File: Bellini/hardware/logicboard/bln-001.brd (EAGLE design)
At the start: 91 x 90 mm, 49 parts, among them IC1 74ACT06N, J1 MKR, J10 THS, J16 MNTR, J2 GPIO, J20 GPIO, J21 Grove, J22 Grove, J23 Grove, J24 Grove, J5 SPI, J6 LED, J7 DIN5, J8 DIN5, J9 DIN5, K1 G5V1, T1 2SC1815, X3 FAN

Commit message: Prototyping...
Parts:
- removed B0: 0, rcl:M3216
- removed C11: 100n, rcl:C025-024X044
- removed C12, C13: 1u, rcl:C050-024X044
- removed D2, D3, D4: (no value), SparkFun-DiscreteSemi:DIODE-1N4148
- removed DISP1: AQM0802A-RN-GBW, AQM0802A-RN-GBW:AQM0802A-RN-GBW-FOOTPRINT
- removed IC1: 74ACT06N, 74xx-eu:DIL14
- removed J1: MKR, SparkFun-Connectors:JST-5-PTH
- removed J10: THS, SparkFun-Connectors:JST-3-PTH-VERT
- removed J16: MNTR, SparkFun-Connectors:JST-2-PTH-NS
- removed J2: GPIO, SparkFun-Connectors:JST-4-PTH
- removed J20: GPIO, SparkFun-Connectors:1X04_1.27MM
- removed J5: SPI, SparkFun-Connectors:1X06_1.27MM
- removed J6: LED, SparkFun-Connectors:JST-3-PTH-VERT
- removed J7, J8, J9: DIN5, SparkFun-Connectors:DIN5-RA-PTH
- removed JP8: Extended GPIO, SparkFun-Connectors:1X10_LOCK
- removed K1: G5V1, relay:G5V1
- removed LED0: Green, led:KA-3528ASYC
- removed LED1: Red, led:KA-3528ASYC
- removed OK1: HCPL2630, optocoupler:DIL08
- removed R1, R4, R5: 1k, resistor:0204/5
- removed R2: 10k, resistor:0204/5
- removed RN2, RN3: 4.7k, resistor-net:RN-5
- removed RN4: 220, resistor-dil:DIL16
- removed T1: 2SC1815, transistor:TO92-ECB
- removed X3: FAN, pinhead:2X02
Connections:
- removed net BASE: R1.1, R2.2, T1.B
- removed net CAP1N: C12.2, DISP1.3
- removed net CAP1P: C12.1, DISP1.4
- removed net COLLECTOR: D2.A, K1.9, T1.C
- removed net COMMON: K1.5, K1.6, X3.2
- removed net FANDRIVE: B0.2, K1.10, X3.4
- removed net LCDVOUT: C13.2, DISP1.2
- removed net LED0A: J6.3, LED0.A, R4.1
- removed net LED1A: J6.1, LED1.A, R5.1
- removed net MIDIINSND: D3.C, OK1.1, RN4.2
- removed net MIRTN: D3.A, J7.5, OK1.2
- removed net MISND: J7.4, RN4.15
- removed net MNTRA: J16.2, RN4.1
- removed net MNTRAA: D4.C, OK1.4, RN4.16
- removed net MNTRK: D4.A, J16.1, OK1.3
- removed net MO2RTN: RN4.9
- removed net MO2RTNRAW: IC1.12, RN4.8
- removed net MO2SND: RN4.10
- removed net MORTN: J9.5, RN4.13
- removed net MORTNRAW: IC1.10, RN4.4
- removed net MOSND: J9.4, RN4.14
- removed net MTRTN: J8.5, RN4.11
- removed net MTRTNRAW: IC1.8, RN4.6
- removed net MTSND: J8.4, RN4.12
- removed net NMO2RTN: IC1.13, IC1.6, RN2.5
- removed net NMORTN: IC1.11, IC1.4, RN2.4
- removed net NMTRTN: IC1.2, IC1.9, RN2.3
- net DIGITAL7: no longer J1.4
- net GND: no longer C11.2, DISP1.6, IC1.7, J1.1, J10.1, J2.1, J5.6, J6.2, J8.2, J9.2, JP8.1, K1.1, LED0.C, LED1.C, OK1.5, R2.1, T1.E, X3.1
- net GPIO0: no longer J2.3, J20.3
- net GPIO1: no longer J2.4, J20.4
- net GPIO2: no longer JP8.3
- net GPIO3: no longer JP8.4
- net GPIO4: no longer JP8.5
- net GPIO5: no longer JP8.6
- net GPIO6: no longer JP8.7
- net GPIO7: no longer JP8.8
- net LED0: no longer R4.2
- net LED1: no longer R5.2
- net MISO: no longer J5.1
- net MNTR: no longer OK1.6, RN3.5
- net MOSI: no longer J5.4
- net RLY: no longer R1.2
- net RST: no longer J5.5
- net RX: no longer IC1.1, OK1.7, RN3.4
- net SCK: no longer J5.3
- net SCL: no longer DISP1.8, J1.3
- net SDA: no longer DISP1.7, J1.2
- net THS: no longer J10.2, RN3.3
- net TX: no longer IC1.3, IC1.5
- net VCC: no longer B0.1, IC1.14, RN2.1, RN4.3, RN4.5, RN4.7, X3.3
- net VDD: no longer C11.1, C13.1, D2.C, DISP1.5, DISP1.9, J1.5, J10.3, J2.2, J5.2, JP8.2, K1.2, OK1.8, RN3.1
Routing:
- net GND: track 479.7 -> 0.00 mm, vias 3 -> 0
- net VDD: track 330.9 -> 0.00 mm, vias 4 -> 0
- net SDA: track 259.0 -> 0.00 mm, vias 4 -> 0
- net SCL: track 238.5 -> 0.00 mm, vias 3 -> 0
- net VCC: track 144.6 -> 0.00 mm, vias 2 -> 0
- net RX: track 140.7 -> 0.00 mm, vias 1 -> 0
- net NMO2RTN: track 123.2 -> 0.00 mm, vias 1 -> 0
- net DIGITAL7: track 117.3 -> 0.00 mm, vias 2 -> 0
- net GPIO3: track 112.9 -> 0.00 mm, vias 2 -> 0
- net GPIO7: track 110.2 -> 0.00 mm, vias 2 -> 0
- net THS: track 106.9 -> 0.00 mm, vias 3 -> 0
- net NMTRTN: track 106.5 -> 0.00 mm, vias 4 -> 0
- net NMORTN: track 102.3 -> 0.00 mm, vias 1 -> 0
- net GPIO6: track 100.3 -> 0.00 mm, vias 2 -> 0
- net TX: track 98.5 -> 0.00 mm
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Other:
- board text removed: "0"
- board text removed: "102"
- board text removed: "104"
- board text removed: "2-472"
- board text removed: "221"
- board text removed: "331"
- board text removed: "4"
- board text removed: "5"
- board text removed: "74HCT05 (5V)"
- board text removed: "Akizuki AQM0802A-RN-GBW"
- board text removed: "BRIDGE*"
- board text removed: "C"
- board text removed: "Configuration of X3"
- board text removed: "DS18B20+"
- board text removed: "Fan GND"
- board text removed: "Fan Vcc"
- board text removed: "G5V-1"
- board text removed: "I"
- board text removed: "L0"
- board text removed: "L1"
- board text removed: "N"
- board text removed: "NO"
- board text removed: "RLY"
- board text removed: "RLY-A"
- board text removed: "RLY-B"
- board text removed: "RTN"
- board text removed: "SND"
- board text removed: "TLP2630"
- board text removed: "TO FAN*"

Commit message: Changed dimension.
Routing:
- removed copper zone on layer 1, net GND
- removed copper zone on layer 16, net GND
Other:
- board size 91 x 90 mm -> 100 x 80 mm
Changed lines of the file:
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@@
 <setting verticaltext="up"/>
 </settings>
-<grid distance="0.5" unitdist="mm" unit="mm" style="lines" multiple="2" display="yes" altdistance="50" altunitdist="mil" altunit="mil"/>
+<grid distance="5" unitdist="mm" unit="mm" style="lines" multiple="2" display="yes" altdistance="50" altunitdist="mil" altunit="mil"/>
 <layers>
 <layer number="1" name="Top" color="4" fill="1" visible="yes" active="yes"/>
@@
 <board>
 <plain>
-<wire x1="78" y1="90" x2="13" y2="90" width="0" layer="20"/>
-<wire x1="13" y1="90" x2="12" y2="89" width="0" layer="20" curve="90"/>
-<wire x1="12" y1="89" x2="12" y2="80" width="0" layer="20"/>
-<wire x1="10.5" y1="78.5" x2="1" y2="78.5" width="0" layer="20"/>
-<wire x1="1" y1="78.5" x2="0" y2="77.5" width="0" layer="20" curve="90"/>
-<wire x1="0" y1="77.5" x2="0" y2="12.5" width="0" layer="20"/>
-<wire x1="0" y1="12.5" x2="1" y2="11.5" width="0" layer="20" curve="90"/>
-<wire x1="1" y1="11.5" x2="10.5" y2="11.5" width="0" layer="20"/>
-<wire x1="12" y1="10" x2="12" y2="1" width="0" layer="20"/>
-<wire x1="12" y1="1" x2="13" y2="0" width="0" layer="20" curve="90"/>
-<wire x1="13" y1="0" x2="78" y2="0" width="0" layer="20"/>
-<wire x1="78" y1="0" x2="79" y2="1" width="0" layer="20" curve="90"/>
-<wire x1="79" y1="1" x2="79" y2="10" width="0" layer="20"/>
-<wire x1="80.5" y1="11.5" x2="90" y2="11.5" width="0" layer="20"/>
-<wire x1="90" y1="11.5" x2="91" y2="12.5" width="0" layer="20" curve="90"/>
-<wire x1="91" y1="12.5" x2="91" y2="77.5" width="0" layer="20"/>
-<wire x1="91" y1="77.5" x2="90" y2="78.5" width="0" layer="20" curve="90"/>
-<wire x1="90" y1="78.5" x2="80.5" y2="78.5" width="0" layer="20"/>
-<wire x1="79" y1="80" x2="79" y2="89" width="0" layer="20"/>
-<wire x1="79" y1="89" x2="78" y2="90" width="0" layer="20" curve="90"/>
+<wire x1="98" y1="80" x2="2" y2="80" width="0" layer="20"/>
+<wire x1="2" y1="80" x2="0" y2="78" width="0" layer="20" curve="90"/>
+<wire x1="0" y1="78" x2="0" y2="2" width="0" layer="20"/>
+<wire x1="0" y1="2" x2="2" y2="0" width="0" layer="20" curve="90"/>
+<wire x1="2" y1="0" x2="98" y2="0" width="0" layer="20"/>
+<wire x1="98" y1="0" x2="100" y2="2" width="0" layer="20" curve="90"/>
+<wire x1="100" y1="2" x2="100" y2="78" width="0" layer="20"/>
+<wire x1="100" y1="78" x2="98" y2="80" width="0" layer="20" curve="90"/>
 <hole x="76.5" y="76" drill="2.5"/>
 <circle x="14.5" y="14" radius="2.6" width="0.2" layer="42"/>
@@
 <circle x="76.5" y="14" radius="2.6" width="0.2" layer="41"/>
 <text x="45.5" y="20.5" size="1.27" layer="25" align="center">Sweetio 0.0.2-X</text>
-<wire x1="79" y1="80" x2="80.5" y2="78.5" width="0" layer="20" curve="90"/>
-<wire x1="12" y1="80" x2="10.5" y2="78.5" width="0" layer="20" curve="-90"/>
-<wire x1="79" y1="10" x2="80.5" y2="11.5" width="0" layer="20" curve="-90"/>
-<wire x1="10.5" y1="11.5" x2="12" y2="10" width="0" layer="20" curve="-90"/>
 <hole x="14.5" y="76" drill="2.5"/>
 <hole x="14.5" y="14" drill="2.5"/>
 <hole x="76.5" y="14" drill="2.5"/>
-<rectangle x1="12" y1="89" x2="79" y2="90" layer="41"/>
-<rectangle x1="90" y1="11.5" x2="91" y2="78.5" layer="41"/>
+<rectangle x1="14" y1="92" x2="81" y2="93" layer="41"/>
+<rectangle x1="115" y1="11.5" x2="116" y2="78.5" layer="41"/>
 <rectangle x1="12" y1="0" x2="79" y2="1" layer="41"/>
-<rectangle x1="0" y1="11.5" x2="1" y2="78.5" layer="41"/>
-<rectangle x1="0" y1="77.5" x2="12" y2="78.5" layer="41"/>
-<rectangle x1="12" y1="78.5" x2="13" y2="90" layer="41"/>
-<rectangle x1="78" y1="78.5" x2="79" y2="90" layer="41"/>
-<rectangle x1="79" y1="77.5" x2="91" y2="78.5" layer="41"/>
-<rectangle x1="79" y1="11.5" x2="91" y2="12.5" layer="41"/>
-<rectangle x1="78" y1="0" x2="79" y2="11.5" layer="41"/>
-<rectangle x1="12" y1="0" x2="13" y2="11.5" layer="41"/>
-<rectangle x1="0" y1="11.5" x2="12" y2="12.5" layer="41"/>
-<rectangle x1="78" y1="0" x2="79" y2="11.5" layer="42"/>
-<rectangle x1="79" y1="11.5" x2="91" y2="12.5" layer="42"/>
-<rectangle x1="90" y1="11.5" x2="91" y2="78.5" layer="42"/>
-<rectangle x1="79" y1="77.5" x2="91" y2="78.5" layer="42"/>
-<rectangle x1="78" y1="78.5" x2="79" y2="90" layer="42"/>
-<rectangle x1="12" y1="89" x2="79" y2="90" layer="42"/>
-<rectangle x1="12" y1="78.5" x2="13" y2="90" layer="42"/>
-<rectangle x1="0" y1="77.5" x2="12" y2="78.5" layer="42"/>
-<rectangle x1="0" y1="11.5" x2="1" y2="78.5" layer="42"/>
-<rectangle x1="0" y1="11.5" x2="12" y2="12.5" layer="42"/>
-<rectangle x1="12" y1="0" x2="13" y2="11.5" layer="42"/>
+<rectangle x1="-10" y1="11.5" x2="-9" y2="78.5" layer="41"/>
+<rectangle x1="-8" y1="90.5" x2="4" y2="91.5" layer="41"/>
+<rectangle x1="4" y1="81" x2="5" y2="92.5" layer="41"/>
+<rectangle x1="85.5" y1="77.5" x2="86.5" y2="89" layer="41"/>
+<rectangle x1="79.5" y1="74" x2="91.5" y2="75" layer="41"/>
+<rectangle x1="76.5" y1="11" x2="88.5" y2="12" layer="41"/>
+<rectangle x1="61" y1="2.5" x2="62" y2="14" layer="41"/>
+<rectangle x1="22" y1="5" x2="23" y2="16.5" layer="41"/>
+<rectangle x1="20" y1="11.5" x2="32" y2="12.5" layer="41"/>
+<rectangle x1="47.5" y1="8" x2="48.5" y2="19.5" layer="42"/>
+<rectangle x1="78" y1="13" x2="90" y2="14" layer="42"/>
+<rectangle x1="110" y1="11.5" x2="111" y2="78.5" layer="42"/>
+<rectangle x1="79.5" y1="75" x2="91.5" y2="76" layer="42"/>
+<rectangle x1="84" y1="78.5" x2="85" y2="90" layer="42"/>
+<rectangle x1="9.5" y1="90.5" x2="76.5" y2="91.5" layer="42"/>
+<rectangle x1="3" y1="82" x2="4" y2="93.5" layer="42"/>
+<rectangle x1="-6" y1="84.5" x2="6" y2="85.5" layer="42"/>
+<rectangle x1="-5" y1="11.5" x2="-4" y2="78.5" layer="42"/>
+<rectangle x1="15" y1="16.5" x2="27" y2="17.5" layer="42"/>
+<rectangle x1="32" y1="5" x2="33" y2="16.5" layer="42"/>
 <rectangle x1="12" y1="0" x2="79" y2="1" layer="42"/>
 <text x="0.5" y="14.5" size="1" layer="25" align="center-left">Designed for
@@
 <contactref element="J23" pad="4"/>
 <contactref element="J24" pad="4"/>
-<polygon width="0.2" layer="1">
-<vertex x="-1" y="-1"/>
-<vertex x="92" y="-1"/>
-<vertex x="92" y="91"/>
-<vertex x="-1" y="91"/>
-</polygon>
-<polygon width="0.2" layer="16">
-<vertex x="-2" y="-2"/>
-<vertex x="93" y="-2"/>
-<vertex x="93" y="92"/>
-<vertex x="-2" y="92"/>
-</polygon>
 <wire x1="58" y1="80.5" x2="69" y2="80.5" width="0" layer="19" extent="1-1"/>
 <wire x1="59.225" y1="64.08" x2="58" y2="80.5" width="0" layer="19" extent="1-1"/>

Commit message: Cleaning.
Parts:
- removed H1, H2: STAND-OFF, SparkFun-Hardware:STAND-OFF
- removed J23, J24: Grove, Connector:4P-2.0-W/O-BUCKLE
- removed JP2: RTC, SparkFun-Connectors:1X05
- removed SV3: Testport II, pinhead:2X07
- added JP01: (no value), pinhead:2X05
- moved J22 80.8 mm to (25.0, 5.50)
- moved J21 79.1 mm to (41.0, 5.50)
- moved C6 70.7 mm to (87.5, 36.0)
- moved LOGO1 63.7 mm to (50.0, 10.0), flipped to the top
- moved U$1 33.3 mm to (50.0, 20.0)
- moved S1 27.7 mm to (50.0, 76.0)
- moved C5 22.4 mm to (75.5, 32.0)
- moved MC2 11.0 mm to (50.0, 64.0)
- moved JP00 4.61 mm to (5.00, 64.0), turned to 90 degrees
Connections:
- net DIGITAL7: no longer SV3.11
- net DTCT0: no longer SV3.8
- net DTCT1: no longer SV3.10
- net DTCT2: no longer SV3.12
- net DTCT3: no longer SV3.14
- net GND: no longer J23.4, J24.4, JP2.2, SV3.5
- net GPIO0: no longer SV3.2
- net GPIO1: no longer SV3.4
- net RX: no longer SV3.3
- net SCL: no longer J23.1, J24.1, JP2.4, SV3.9
- net SDA: no longer J23.2, J24.2, JP2.5, SV3.7
- net THS: no longer SV3.6
- net TX: no longer SV3.1
- net VDD: no longer J23.3, J24.3, JP2.1, SV3.13
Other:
- board text added: "Bellini Prototype 00"
- board text removed: "1"
- board text removed: "2"
- board text removed: "2-Grove"
- board text removed: "SC"
- board text removed: "SD"
- board text removed: "SparkFun Real Time Clock Module (12708)"
- board text removed: "Sweetio 0.0.2-X"
- board text removed: "TestPort II"
- board text removed: "To RUN Pad (RPiZW2)"

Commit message: Layout.
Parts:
- removed J22: Grove, Connector:4P-2.0-90D
- added JP02, JP03: (no value), adafruit:1X08-BIG
- added JP04, JP05: (no value), pinhead:1X14
- moved JP01 70.0 mm to (15.0, 20.0)
- moved C6 61.0 mm to (27.5, 25.0)
- moved C7 60.8 mm to (14.5, 64.0)
- moved J21 26.2 mm to (15.0, 9.00), turned to 180 degrees
- moved U$1 20.0 mm to (50.0, 40.0), flipped to the bottom
- moved C5 14.2 mm to (81.2, 45.0)
- moved LOGO1 7.00 mm to (50.0, 3.00)
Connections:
- net GND: no longer J22.4
- net SCL: no longer J22.1
- net SDA: no longer J22.2
- net VDD: no longer J22.3

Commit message: Routed.
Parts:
- removed JP01: (no value), pinhead:2X05
- added LEVELSHIFT1, LEVELSHIFT2: (no value), pinhead:1X04
- added RTCPIN: (no value), pinhead:2X05
- turned DRIVERPIN1 to 270 degrees
- turned LEDPIN2 to 270 degrees
- renumbered J21 to GROVE1, JP02 to LEDPIN1, JP03 to LEDPIN2, JP04 to DRIVERPIN1, JP05 to DRIVERPIN2
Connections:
- removed net DTCT0: MC2.15
- removed net DTCT1: MC2.16
- removed net DTCT2: MC2.18
- removed net DTCT3: MC2.22
- removed net GPIO0: MC2.38
- removed net GPIO1: MC2.40
- removed net GPIO2: MC2.24
- removed net GPIO3: MC2.36
- removed net GPIO4: MC2.11
- removed net GPIO5: MC2.12
- removed net GPIO6: MC2.35
- removed net GPIO7: MC2.37
- removed net LED0: MC2.32
- removed net LED1: MC2.33
- removed net MISO: MC2.21
- removed net MNTR: MC2.31
- removed net MOSI: MC2.19
- removed net RLY: MC2.29
- removed net SCK: MC2.23
- removed net THS: MC2.7
- new net COL1: DRIVERPIN2.11, LEDPIN2.5
- new net COL2: DRIVERPIN2.10, LEDPIN1.3
- new net COL3: DRIVERPIN2.9, LEDPIN1.4
- new net COL4: DRIVERPIN2.8, LEDPIN2.3
- new net COL5: DRIVERPIN2.7, LEDPIN1.6
- new net COL6: DRIVERPIN2.6
- new net COL7: DRIVERPIN2.5, LEDPIN2.7
- new net COL8: DRIVERPIN2.4, LEDPIN2.8
- new net N$10: DRIVERPIN1.11
- new net N$11: DRIVERPIN1.12
- new net N$12: DRIVERPIN1.13
- new net N$13: DRIVERPIN1.14
- new net N$14: DRIVERPIN2.1
- new net N$15: DRIVERPIN2.2
- new net N$16: DRIVERPIN2.3
- new net N$5: LEVELSHIFT1.4
- new net N$9: DRIVERPIN1.10
- new net ROW1: DRIVERPIN1.2, LEDPIN2.1
- new net ROW2: DRIVERPIN1.3, LEDPIN2.6
- new net ROW3: DRIVERPIN1.4, LEDPIN1.8
- new net ROW4: DRIVERPIN1.5, LEDPIN2.4
- new net ROW5: DRIVERPIN1.6, LEDPIN1.1
- new net ROW6: DRIVERPIN1.7, LEDPIN1.7
- new net ROW7: DRIVERPIN1.8, LEDPIN1.2, LEDPIN2.2
- new net ROW8: DRIVERPIN1.9, LEDPIN1.5
- new net SCL5V: DRIVERPIN2.12, LEVELSHIFT2.3
- new net SDA5V: DRIVERPIN2.13, LEVELSHIFT2.2
- net DIGITAL7: now also RTCPIN.7
- net GND: now also DRIVERPIN1.1, LEVELSHIFT2.1, RTCPIN.6, RTCPIN.9; no longer MC2.25
- net RX: now also RTCPIN.10
- net SCL: now also LEVELSHIFT1.2, RTCPIN.5
- net SDA: now also LEVELSHIFT1.3, RTCPIN.3
- net TX: now also RTCPIN.8
- net VCC: now also DRIVERPIN2.14, LEVELSHIFT2.4, RTCPIN.2, RTCPIN.4
- net VDD: now also LEVELSHIFT1.1, RTCPIN.1
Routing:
- net GND: track 0.00 -> 227.3 mm
- net VDD: track 0.00 -> 176.4 mm
- net SCL: track 0.00 -> 115.4 mm
- net SDA: track 0.00 -> 114.3 mm
- net VCC: track 0.00 -> 103.0 mm
- net COL5: track 0.00 -> 69.5 mm
- net COL2: track 0.00 -> 68.2 mm
- net COL3: track 0.00 -> 66.0 mm
- net TX: track 0.00 -> 61.9 mm
- net RX: track 0.00 -> 59.1 mm
- net RST: track 0.00 -> 54.3 mm
- net ROW7: track 0.00 -> 50.4 mm
- net ROW5: track 0.00 -> 49.1 mm
- net ROW6: track 0.00 -> 39.6 mm
- net ROW8: track 0.00 -> 38.7 mm
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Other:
- board text added: "1"
- board text added: "4-M3"
- board text added: "Bellini Prototype 00 v1.0"
- board text added: "Designed for Takachi SKL10-5-10"
- board text added: "HT16K33 Breakout"
- board text added: "OptoSuply OSL641501"
- board text added: "PCA9306 Breakout"
- board text removed: "103"
- board text removed: "4-M2.3"
- board text removed: "Bellini Prototype 00"
- board text removed: "Designed for Takachi PF10-4-10"

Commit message: Fixed errors.
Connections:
- net COL1 renamed A0
- net COL2 renamed A1
- net COL3 renamed A2
- net COL5 renamed A4
- net COL7 renamed A6
- net COL8 renamed A7
- net ROW1 renamed C0
- net ROW2 renamed C1
- net ROW3 renamed C2
- net ROW4 renamed C3
- net ROW5 renamed C4
- net ROW6 renamed C5
- net ROW8 renamed C7
- removed net COL4: DRIVERPIN2.8, LEDPIN2.3
- removed net COL6: DRIVERPIN2.6
- removed net ROW7: DRIVERPIN1.8, LEDPIN1.2, LEDPIN2.2
- new net A3: DRIVERPIN2.8, LEDPIN2.2
- new net A5: DRIVERPIN2.6, LEDPIN2.3
- new net C6: DRIVERPIN1.8, LEDPIN1.2
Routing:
- net ROW7: track 50.4 -> 0.00 mm
- net C6: track 0.00 -> 38.7 mm
- net A5: track 0.00 -> 32.1 mm
- net COL4: track 30.0 -> 0.00 mm
- net A3: track 0.00 -> 29.2 mm
- net VDD: track 176.4 -> 162.1 mm, vias 0 -> 2
- net SCL: track 115.4 -> 119.3 mm
- net SDA: track 114.3 -> 117.8 mm
- net A2: track 66.0 -> 69.4 mm
- net TX: track 61.9 -> 59.9 mm, vias 0 -> 1
- net DIGITAL7: track 35.2 -> 36.7 mm
- net A0: track 37.1 -> 38.4 mm
- added copper zone on layer 1, net GND
- added copper zone on layer 16, net GND

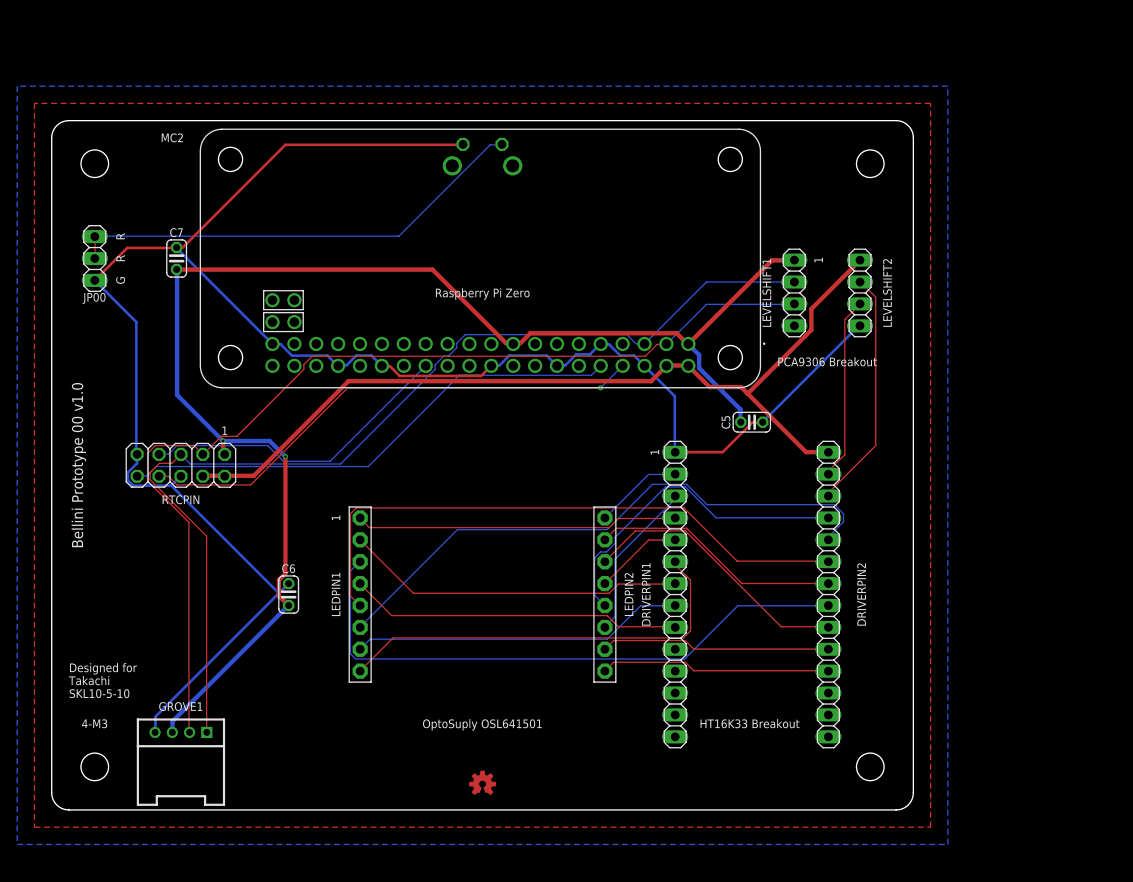
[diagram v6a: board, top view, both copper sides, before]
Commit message: Fixed direction of Pi RTC.
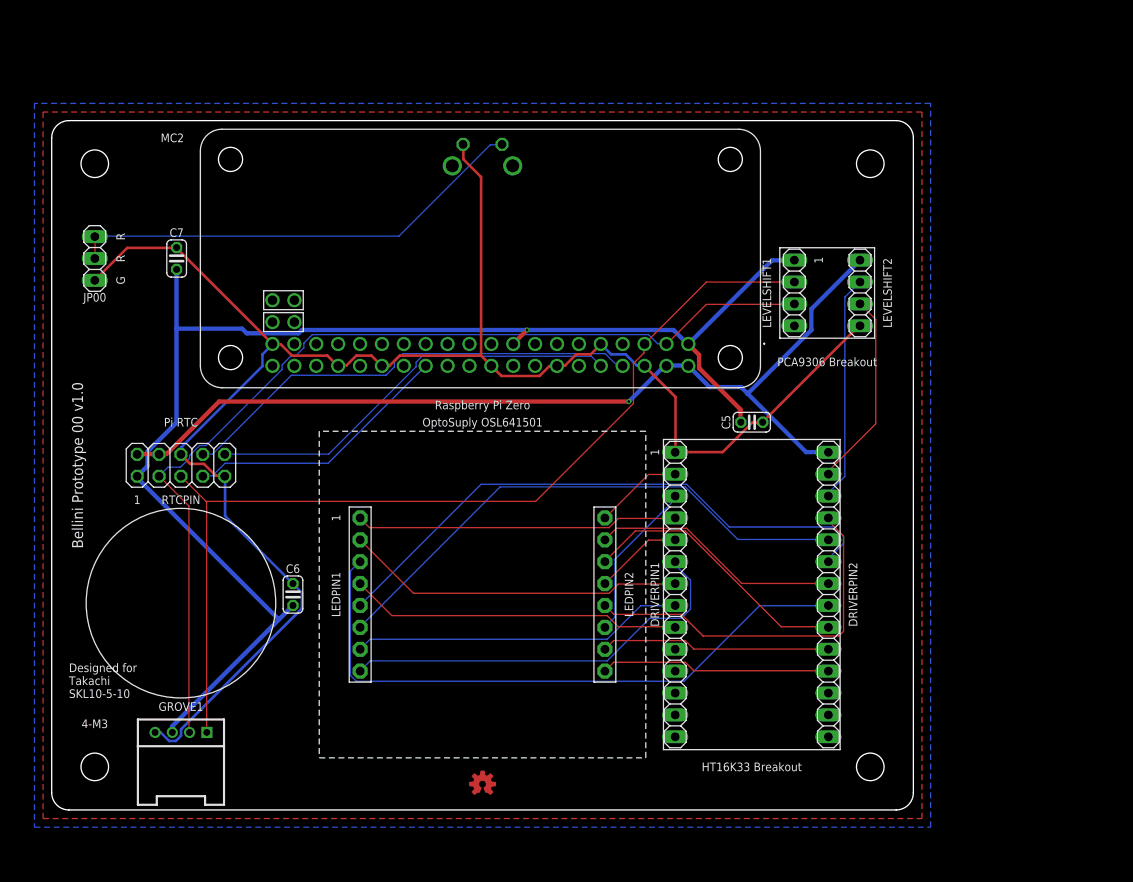
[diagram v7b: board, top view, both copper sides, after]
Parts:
- moved C6 0.50 mm to (28.0, 25.0)
- turned RTCPIN to 0 degrees
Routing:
- net GND: track 227.3 -> 207.3 mm
- net RX: track 59.1 -> 49.1 mm
- net VCC: track 103.0 -> 109.5 mm, vias 0 -> 1
- net SCL: track 119.3 -> 113.1 mm
- net DIGITAL7: track 36.7 -> 31.2 mm
- net TX: track 59.9 -> 54.5 mm, vias 1 -> 0
- net A0: track 38.4 -> 43.3 mm
- net A1: track 68.2 -> 63.7 mm
- net A4: track 69.5 -> 73.1 mm
- net SDA: track 117.8 -> 115.0 mm
- net VDD: track 162.1 -> 160.5 mm, vias 2 -> 1
- net SCL5V: track 27.9 -> 26.4 mm
- net SDA5V: track 21.3 -> 22.8 mm
- net C4: track 49.1 -> 47.6 mm
- net A2: track 69.4 -> 68.1 mm
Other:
- board text added: "Pi RTC"
